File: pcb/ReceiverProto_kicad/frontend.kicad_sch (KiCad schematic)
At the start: 32 parts, among them Q1 Q_NPN_BCE, Q2 NJFET, Q3 NJFET, U1 AD8001AN, U3 MAX40079AUT_T

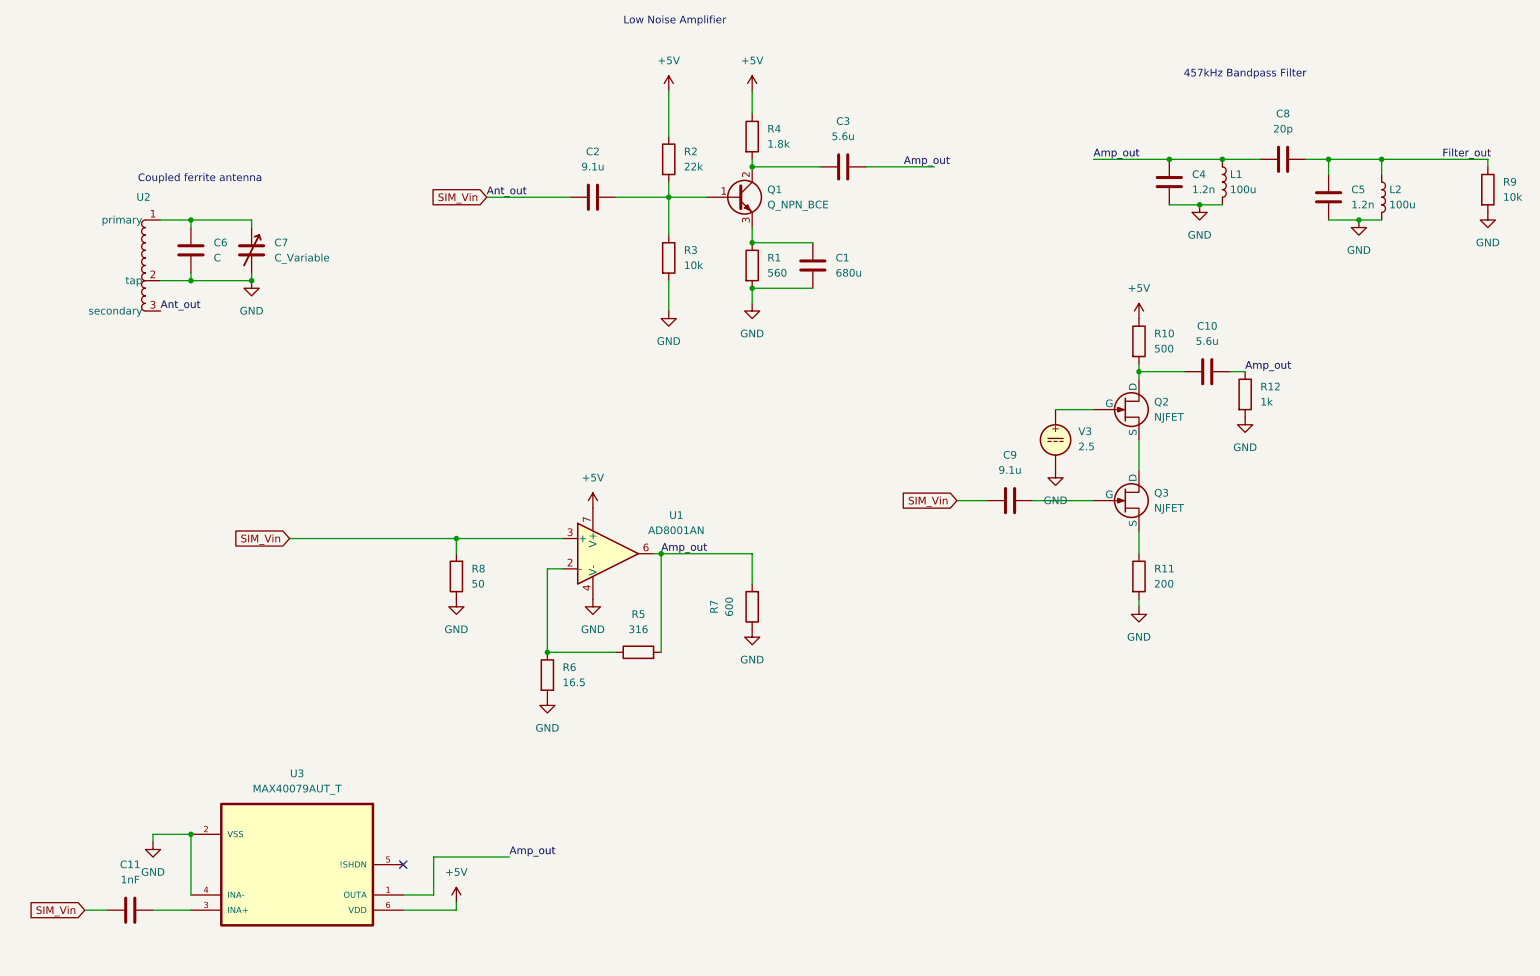
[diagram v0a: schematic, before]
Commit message: created 3.3V voltage regulator circuit, as well implemented the amplifier in the frontend.
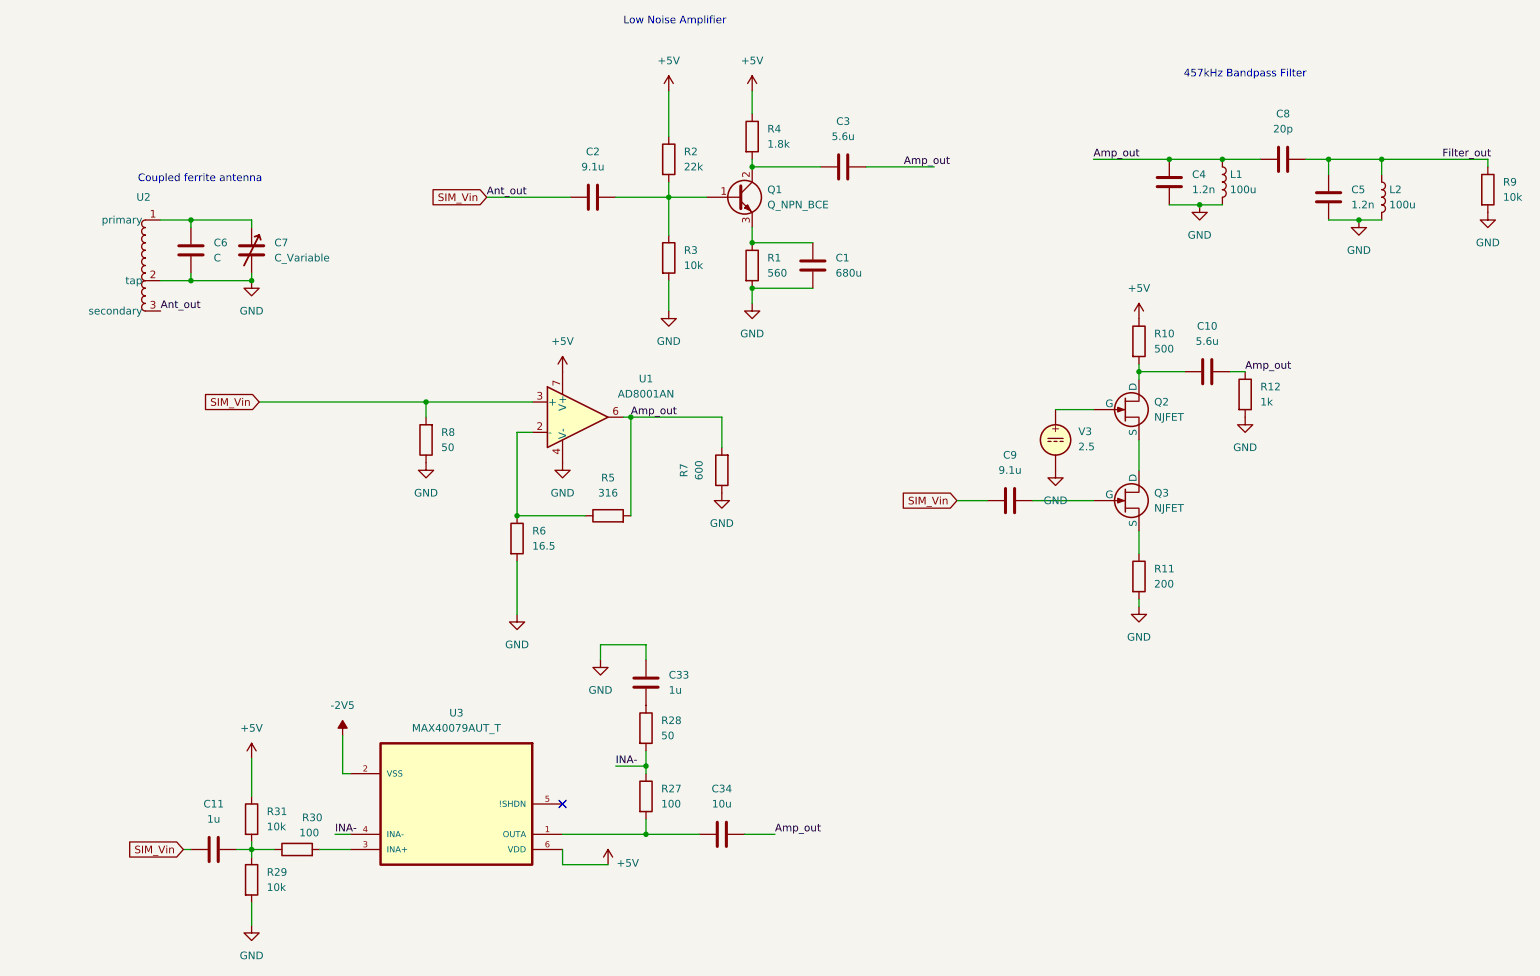
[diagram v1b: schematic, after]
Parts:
- added C33: 1u, symbol Device:C
- added C34: 10u, symbol Device:C
- added R27, R30: 100, symbol Device:R
- added R28: 50, symbol Device:R
- added R29, R31: 10k, symbol Device:R
- C11: value 1nF -> 1u
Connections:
- net +5V: now also R31.1
- net Amp_out: now also C34.2; no longer U3.1 (OUTA)
- net GND: now also C33.1, R29.2; no longer U3.2 (VSS), U3.4 (INA-)
- net at C11.2: now also R29.1, R30.1, R31.2; no longer U3.3 (INA+)
- new net: C33.2, R28.1
- new net: R30.2, U3.3 (INA+)
- new net: C34.1, R27.2, U3.1 (OUTA)
- new net -2V5: U3.2 (VSS)
- new net INA-: R27.1, R28.2, U3.4 (INA-)
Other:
- moved on the sheet: R5, R6, R7, R8, U1, U3

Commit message: changes to adc drivers.
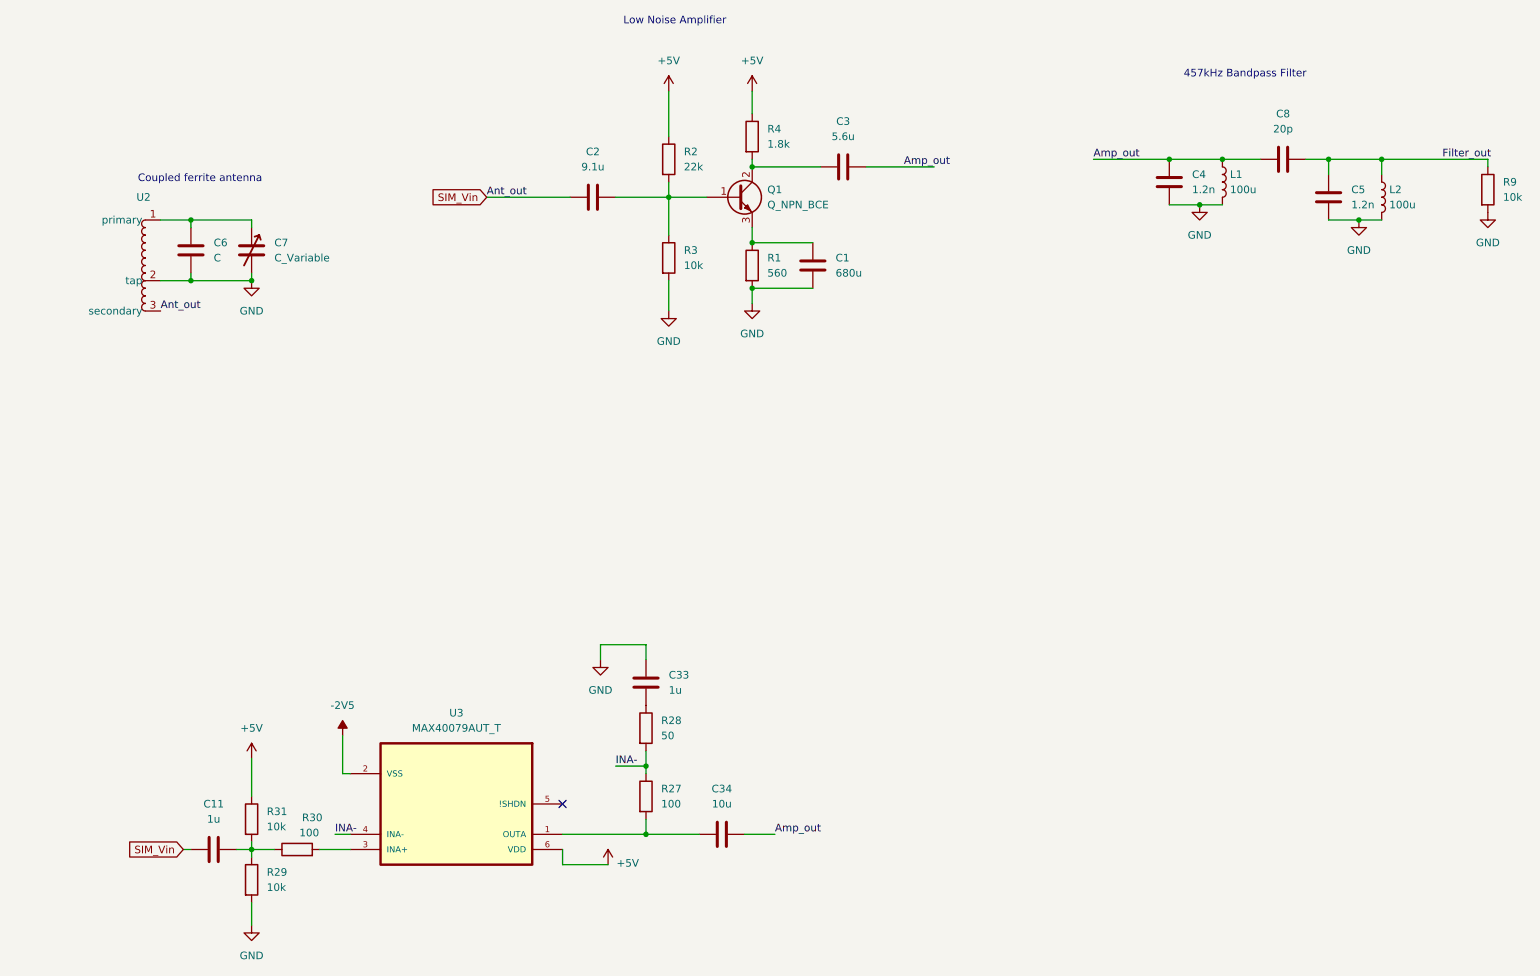
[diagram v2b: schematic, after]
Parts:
- removed C10: 5.6u, symbol Device:C
- removed C9: 9.1u, symbol Device:C
- removed Q2, Q3: NJFET, symbol Simulation_SPICE:NJFET
- removed R10: 500, symbol Device:R
- removed R11: 200, symbol Device:R
- removed R12: 1k, symbol Device:R
- removed R5: 316, symbol Device:R
- removed R6: 16.5, symbol Device:R
- removed R7: 600, symbol Device:R
- removed R8: 50, symbol Device:R
- removed U1: AD8001AN, Package_DIP:DIP-8_W7.62mm, symbol Amplifier_Operational:AD8001AN
- removed V3: 2.5, symbol Simulation_SPICE:VDC

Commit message: add footprints for remaining symbols; 3.3V regulator still needs footprint
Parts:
- C1, C11, C2, C3, C33, C34, C4, C5, C6, C7, C8, L1, L2, Q1, R1, R2, R27, R28, R29, R3, R30, R31, R4, R9, U2, U3: now left out of the parts list
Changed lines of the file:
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@@
 		(unit 1)
 		(exclude_from_sim no)
-		(in_bom yes)
-		(on_board yes)
+		(in_bom no)
+		(on_board no)
 		(dnp no)
 		(property "Reference" "#PWR072"
@@
 		(unit 1)
 		(exclude_from_sim no)
-		(in_bom yes)
-		(on_board yes)
+		(in_bom no)
+		(on_board no)
 		(dnp no)
 		(fields_autoplaced yes)
@@
 		(unit 1)
 		(exclude_from_sim yes)
-		(in_bom yes)
-		(on_board yes)
+		(in_bom no)
+		(on_board no)
 		(dnp no)
 		(fields_autoplaced yes)
@@
 		(unit 1)
 		(exclude_from_sim yes)
-		(in_bom yes)
-		(on_board yes)
+		(in_bom no)
+		(on_board no)
 		(dnp no)
 		(fields_autoplaced yes)
@@
 		(unit 1)
 		(exclude_from_sim yes)
-		(in_bom yes)
-		(on_board yes)
+		(in_bom no)
+		(on_board no)
 		(dnp no)
 		(fields_autoplaced yes)
@@
 		(unit 1)
 		(exclude_from_sim yes)
-		(in_bom yes)
-		(on_board yes)
+		(in_bom no)
+		(on_board no)
 		(dnp no)
 		(fields_autoplaced yes)
@@
 		(unit 1)
 		(exclude_from_sim yes)
-		(in_bom yes)
-		(on_board yes)
+		(in_bom no)
+		(on_board no)
 		(dnp no)
 		(fields_autoplaced yes)
@@
 		(unit 1)
 		(exclude_from_sim yes)
-		(in_bom yes)
-		(on_board yes)
+		(in_bom no)
+		(on_board no)
 		(dnp no)
 		(fields_autoplaced yes)
@@
 		(unit 1)
 		(exclude_from_sim yes)
-		(in_bom yes)
-		(on_board yes)
+		(in_bom no)
+		(on_board no)
 		(dnp no)
 		(fields_autoplaced yes)
@@
 		(unit 1)
 		(exclude_from_sim no)
-		(in_bom yes)
-		(on_board yes)
+		(in_bom no)
+		(on_board no)
 		(dnp no)
 		(fields_autoplaced yes)
@@
 		(unit 1)
 		(exclude_from_sim yes)
-		(in_bom yes)
-		(on_board yes)
+		(in_bom no)
+		(on_board no)
 		(dnp no)
 		(fields_autoplaced yes)
@@
 		(unit 1)
 		(exclude_from_sim yes)
-		(in_bom yes)
-		(on_board yes)
+		(in_bom no)
+		(on_board no)
 		(dnp no)
 		(fields_autoplaced yes)
@@
 		(unit 1)
 		(exclude_from_sim yes)
-		(in_bom yes)
-		(on_board yes)
+		(in_bom no)
+		(on_board no)
 		(dnp no)
 		(fields_autoplaced yes)
@@
 		(unit 1)
 		(exclude_from_sim yes)
-		(in_bom yes)
-		(on_board yes)
+		(in_bom no)
+		(on_board no)
 		(dnp no)
 		(fields_autoplaced yes)
@@
 		(unit 1)
 		(exclude_from_sim yes)
-		(in_bom yes)
-		(on_board yes)
+		(in_bom no)
+		(on_board no)
 		(dnp no)
 		(fields_autoplaced yes)
@@
 		(unit 1)
 		(exclude_from_sim yes)
-		(in_bom yes)
-		(on_board yes)
+		(in_bom no)
+		(on_board no)
 		(dnp no)
 		(fields_autoplaced yes)
@@
 		(unit 1)
 		(exclude_from_sim yes)
-		(in_bom yes)
-		(on_board yes)
+		(in_bom no)
+		(on_board no)
 		(dnp no)
 		(fields_autoplaced yes)
@@
 		(unit 1)
 		(exclude_from_sim yes)
-		(in_bom yes)
-		(on_board yes)
+		(in_bom no)
+		(on_board no)
 		(dnp no)
 		(fields_autoplaced yes)
@@
 		(unit 1)
 		(exclude_from_sim no)
-		(in_bom yes)
-		(on_board yes)
+		(in_bom no)
+		(on_board no)
 		(dnp no)
 		(fields_autoplaced yes)
@@
 		(unit 1)
 		(exclude_from_sim yes)
-		(in_bom yes)
-		(on_board yes)
+		(in_bom no)
+		(on_board no)
 		(dnp no)
 		(fields_autoplaced yes)
@@
 		(unit 1)
 		(exclude_from_sim no)
-		(in_bom yes)
-		(on_board yes)
+		(in_bom no)
+		(on_board no)
 		(dnp no)
 		(fields_autoplaced yes)
@@
 		(unit 1)
 		(exclude_from_sim no)
-		(in_bom yes)
-		(on_board yes)
+		(in_bom no)
+		(on_board no)
 		(dnp no)
 		(fields_autoplaced yes)
@@
 		(unit 1)
 		(exclude_from_sim yes)
-		(in_bom yes)
-		(on_board yes)
+		(in_bom no)
+		(on_board no)
 		(dnp no)
 		(fields_autoplaced yes)
@@
 		(unit 1)
 		(exclude_from_sim no)
-		(in_bom yes)
-		(on_board yes)
+		(in_bom no)
+		(on_board no)
 		(dnp no)
 		(fields_autoplaced yes)
@@
 		(unit 1)
 		(exclude_from_sim yes)
-		(in_bom yes)
-		(on_board yes)
+		(in_bom no)
+		(on_board no)
 		(dnp no)
 		(fields_autoplaced yes)
@@
 		(unit 1)
 		(exclude_from_sim no)
-		(in_bom yes)
-		(on_board yes)
+		(in_bom no)
+		(on_board no)
 		(dnp no)
 		(fields_autoplaced yes)
@@
 		(unit 1)
 		(exclude_from_sim yes)
-		(in_bom yes)
-		(on_board yes)
+		(in_bom no)
+		(on_board no)
 		(dnp no)
 		(fields_autoplaced yes)
@@
 		(unit 1)
 		(exclude_from_sim yes)
-		(in_bom yes)
-		(on_board yes)
+		(in_bom no)
+		(on_board no)
 		(dnp no)
 		(fields_autoplaced yes)
@@
 		(unit 1)
 		(exclude_from_sim yes)
-		(in_bom yes)
-		(on_board yes)
+		(in_bom no)
+		(on_board no)
 		(dnp no)
 		(fields_autoplaced yes)
@@
 		(unit 1)
 		(exclude_from_sim no)
-		(in_bom yes)
-		(on_board yes)
+		(in_bom no)
+		(on_board no)
 		(dnp no)
 		(fields_autoplaced yes)
@@
 		(unit 1)
 		(exclude_from_sim yes)
-		(in_bom yes)
-		(on_board yes)
+		(in_bom no)
+		(on_board no)
 		(dnp no)
 		(fields_autoplaced yes)
@@
 		(unit 1)
 		(exclude_from_sim yes)
-		(in_bom yes)
-		(on_board yes)
+		(in_bom no)
+		(on_board no)
 		(dnp no)
 		(fields_autoplaced yes)
@@
 		(unit 1)
 		(exclude_from_sim no)
-		(in_bom yes)
-		(on_board yes)
+		(in_bom no)
+		(on_board no)
 		(dnp no)
 		(property "Reference" "R30"
@@
 		(unit 1)
 		(exclude_from_sim yes)
-		(in_bom yes)
-		(on_board yes)
+		(in_bom no)
+		(on_board no)
 		(dnp no)
 		(fields_autoplaced yes)
@@
 		(unit 1)
 		(exclude_from_sim no)
-		(in_bom yes)
-		(on_board yes)
+		(in_bom no)
+		(on_board no)
 		(dnp no)
 		(fields_autoplaced yes)
@@
 		(unit 1)
 		(exclude_from_sim no)
-		(in_bom yes)
-		(on_board yes)
+		(in_bom no)
+		(on_board no)
 		(dnp no)
 		(fields_autoplaced yes)
@@
 		(unit 1)
 		(exclude_from_sim no)
-		(in_bom yes)
-		(on_board yes)
+		(in_bom no)
+		(on_board no)
 		(dnp no)
 		(fields_autoplaced yes)
@@
 		(unit 1)
 		(exclude_from_sim no)
-		(in_bom yes)
-		(on_board yes)
+		(in_bom no)
+		(on_board no)
 		(dnp no)
 		(fields_autoplaced yes)
@@
 		(unit 1)
 		(exclude_from_sim yes)
-		(in_bom yes)
-		(on_board yes)
-		(dnp no)
-		(fields_autoplaced yes)
+		(in_bom no)
+		(on_board no)
+		(dnp no)
+		(fields_autoplaced yes)

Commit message: Fixed footprint for voltage regulator.
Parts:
- C1, C11, C2, C3, C33, C34, C4, C5, C6, C7, C8, L1, L2, Q1, R1, R2, R27, R28, R29, R3, R30, R31, R4, R9, U2, U3: now in the parts list
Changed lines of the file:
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@@
 		(unit 1)
 		(exclude_from_sim no)
-		(in_bom no)
-		(on_board no)
+		(in_bom yes)
+		(on_board yes)
 		(dnp no)
 		(property "Reference" "#PWR072"
@@
 		(unit 1)
 		(exclude_from_sim no)
-		(in_bom no)
-		(on_board no)
+		(in_bom yes)
+		(on_board yes)
 		(dnp no)
 		(fields_autoplaced yes)
@@
 		(unit 1)
 		(exclude_from_sim yes)
-		(in_bom no)
-		(on_board no)
+		(in_bom yes)
+		(on_board yes)
 		(dnp no)
 		(fields_autoplaced yes)
@@
 		(unit 1)
 		(exclude_from_sim yes)
-		(in_bom no)
-		(on_board no)
+		(in_bom yes)
+		(on_board yes)
 		(dnp no)
 		(fields_autoplaced yes)
@@
 		(unit 1)
 		(exclude_from_sim yes)
-		(in_bom no)
-		(on_board no)
+		(in_bom yes)
+		(on_board yes)
 		(dnp no)
 		(fields_autoplaced yes)
@@
 		(unit 1)
 		(exclude_from_sim yes)
-		(in_bom no)
-		(on_board no)
+		(in_bom yes)
+		(on_board yes)
 		(dnp no)
 		(fields_autoplaced yes)
@@
 		(unit 1)
 		(exclude_from_sim yes)
-		(in_bom no)
-		(on_board no)
+		(in_bom yes)
+		(on_board yes)
 		(dnp no)
 		(fields_autoplaced yes)
@@
 		(unit 1)
 		(exclude_from_sim yes)
-		(in_bom no)
-		(on_board no)
+		(in_bom yes)
+		(on_board yes)
 		(dnp no)
 		(fields_autoplaced yes)
@@
 		(unit 1)
 		(exclude_from_sim yes)
-		(in_bom no)
-		(on_board no)
+		(in_bom yes)
+		(on_board yes)
 		(dnp no)
 		(fields_autoplaced yes)
@@
 		(unit 1)
 		(exclude_from_sim no)
-		(in_bom no)
-		(on_board no)
+		(in_bom yes)
+		(on_board yes)
 		(dnp no)
 		(fields_autoplaced yes)
@@
 		(unit 1)
 		(exclude_from_sim yes)
-		(in_bom no)
-		(on_board no)
+		(in_bom yes)
+		(on_board yes)
 		(dnp no)
 		(fields_autoplaced yes)
@@
 		(unit 1)
 		(exclude_from_sim yes)
-		(in_bom no)
-		(on_board no)
+		(in_bom yes)
+		(on_board yes)
 		(dnp no)
 		(fields_autoplaced yes)
@@
 		(unit 1)
 		(exclude_from_sim yes)
-		(in_bom no)
-		(on_board no)
+		(in_bom yes)
+		(on_board yes)
 		(dnp no)
 		(fields_autoplaced yes)
@@
 		(unit 1)
 		(exclude_from_sim yes)
-		(in_bom no)
-		(on_board no)
+		(in_bom yes)
+		(on_board yes)
 		(dnp no)
 		(fields_autoplaced yes)
@@
 		(unit 1)
 		(exclude_from_sim yes)
-		(in_bom no)
-		(on_board no)
+		(in_bom yes)
+		(on_board yes)
 		(dnp no)
 		(fields_autoplaced yes)
@@
 		(unit 1)
 		(exclude_from_sim yes)
-		(in_bom no)
-		(on_board no)
+		(in_bom yes)
+		(on_board yes)
 		(dnp no)
 		(fields_autoplaced yes)
@@
 		(unit 1)
 		(exclude_from_sim yes)
-		(in_bom no)
-		(on_board no)
+		(in_bom yes)
+		(on_board yes)
 		(dnp no)
 		(fields_autoplaced yes)
@@
 		(unit 1)
 		(exclude_from_sim yes)
-		(in_bom no)
-		(on_board no)
+		(in_bom yes)
+		(on_board yes)
 		(dnp no)
 		(fields_autoplaced yes)
@@
 		(unit 1)
 		(exclude_from_sim no)
-		(in_bom no)
-		(on_board no)
+		(in_bom yes)
+		(on_board yes)
 		(dnp no)
 		(fields_autoplaced yes)
@@
 		(unit 1)
 		(exclude_from_sim yes)
-		(in_bom no)
-		(on_board no)
+		(in_bom yes)
+		(on_board yes)
 		(dnp no)
 		(fields_autoplaced yes)
@@
 		(unit 1)
 		(exclude_from_sim no)
-		(in_bom no)
-		(on_board no)
+		(in_bom yes)
+		(on_board yes)
 		(dnp no)
 		(fields_autoplaced yes)
@@
 		(unit 1)
 		(exclude_from_sim no)
-		(in_bom no)
-		(on_board no)
+		(in_bom yes)
+		(on_board yes)
 		(dnp no)
 		(fields_autoplaced yes)
@@
 		(unit 1)
 		(exclude_from_sim yes)
-		(in_bom no)
-		(on_board no)
+		(in_bom yes)
+		(on_board yes)
 		(dnp no)
 		(fields_autoplaced yes)
@@
 		(unit 1)
 		(exclude_from_sim no)
-		(in_bom no)
-		(on_board no)
+		(in_bom yes)
+		(on_board yes)
 		(dnp no)
 		(fields_autoplaced yes)
@@
 		(unit 1)
 		(exclude_from_sim yes)
-		(in_bom no)
-		(on_board no)
+		(in_bom yes)
+		(on_board yes)
 		(dnp no)
 		(fields_autoplaced yes)
@@
 		(unit 1)
 		(exclude_from_sim no)
-		(in_bom no)
-		(on_board no)
+		(in_bom yes)
+		(on_board yes)
 		(dnp no)
 		(fields_autoplaced yes)
@@
 		(unit 1)
 		(exclude_from_sim yes)
-		(in_bom no)
-		(on_board no)
+		(in_bom yes)
+		(on_board yes)
 		(dnp no)
 		(fields_autoplaced yes)
@@
 		(unit 1)
 		(exclude_from_sim yes)
-		(in_bom no)
-		(on_board no)
+		(in_bom yes)
+		(on_board yes)
 		(dnp no)
 		(fields_autoplaced yes)
@@
 		(unit 1)
 		(exclude_from_sim yes)
-		(in_bom no)
-		(on_board no)
+		(in_bom yes)
+		(on_board yes)
 		(dnp no)
 		(fields_autoplaced yes)
@@
 		(unit 1)
 		(exclude_from_sim no)
-		(in_bom no)
-		(on_board no)
+		(in_bom yes)
+		(on_board yes)
 		(dnp no)
 		(fields_autoplaced yes)
@@
 		(unit 1)
 		(exclude_from_sim yes)
-		(in_bom no)
-		(on_board no)
+		(in_bom yes)
+		(on_board yes)
 		(dnp no)
 		(fields_autoplaced yes)
@@
 		(unit 1)
 		(exclude_from_sim yes)
-		(in_bom no)
-		(on_board no)
+		(in_bom yes)
+		(on_board yes)
 		(dnp no)
 		(fields_autoplaced yes)
@@
 		(unit 1)
 		(exclude_from_sim no)
-		(in_bom no)
-		(on_board no)
+		(in_bom yes)
+		(on_board yes)
 		(dnp no)
 		(property "Reference" "R30"
@@
 		(unit 1)
 		(exclude_from_sim yes)
-		(in_bom no)
-		(on_board no)
+		(in_bom yes)
+		(on_board yes)
 		(dnp no)
 		(fields_autoplaced yes)
@@
 		(unit 1)
 		(exclude_from_sim no)
-		(in_bom no)
-		(on_board no)
+		(in_bom yes)
+		(on_board yes)
 		(dnp no)
 		(fields_autoplaced yes)
@@
 		(unit 1)
 		(exclude_from_sim no)
-		(in_bom no)
-		(on_board no)
+		(in_bom yes)
+		(on_board yes)
 		(dnp no)
 		(fields_autoplaced yes)
@@
 		(unit 1)
 		(exclude_from_sim no)
-		(in_bom no)
-		(on_board no)
+		(in_bom yes)
+		(on_board yes)
 		(dnp no)
 		(fields_autoplaced yes)
@@
 		(unit 1)
 		(exclude_from_sim no)
-		(in_bom no)
-		(on_board no)
+		(in_bom yes)
+		(on_board yes)
 		(dnp no)
 		(fields_autoplaced yes)
@@
 		(unit 1)
 		(exclude_from_sim yes)
-		(in_bom no)
-		(on_board no)
-		(dnp no)
-		(fields_autoplaced yes)
+		(in_bom yes)
+		(on_board yes)
+		(dnp no)
+		(fields_autoplaced yes)
